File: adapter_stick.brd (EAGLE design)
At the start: 15.2 x 20 mm, 7 parts, among them J1X CLONOLU

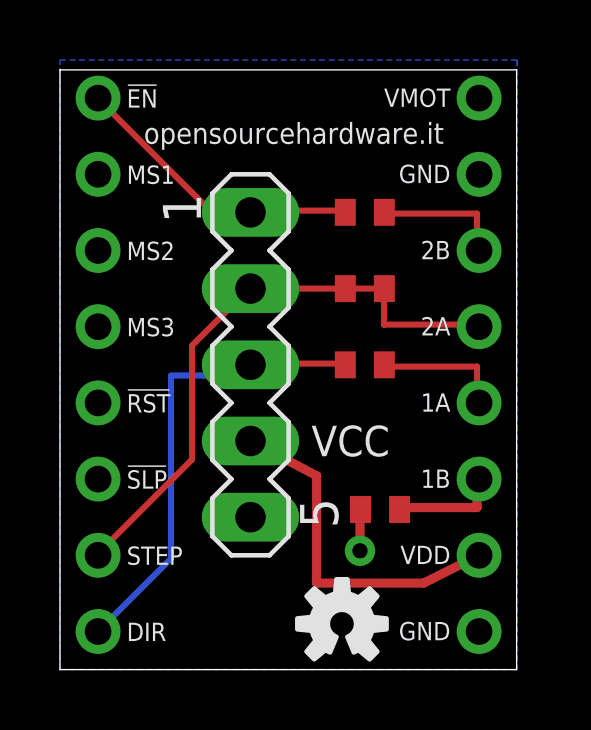
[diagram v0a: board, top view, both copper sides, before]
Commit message: BUG in board (DIR jumper shorted)
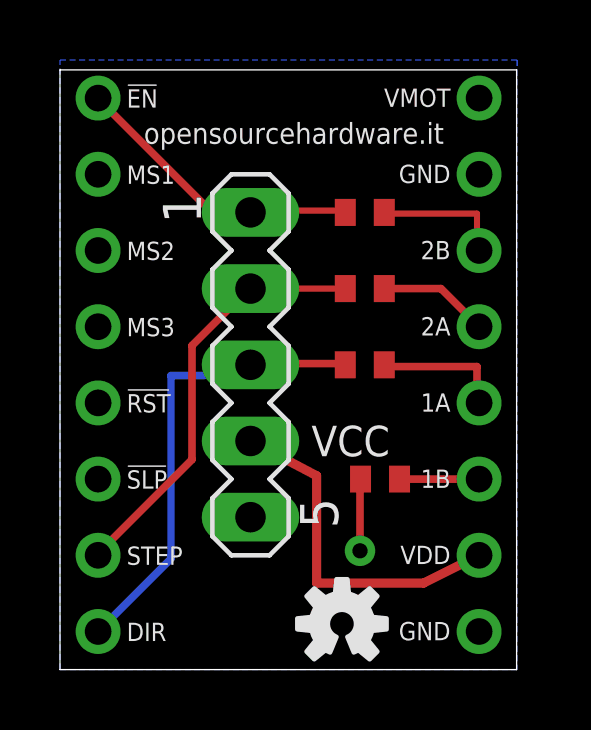
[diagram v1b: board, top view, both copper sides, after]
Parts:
- moved R5 1.02 mm to (10.7, 6.35)
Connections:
- new net 2A: J1X.2A, R3.2
- net NC: no longer J1X.2A, R3.2
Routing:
- net NC: track 19.9 -> 14.2 mm
- net 2A: track 0.00 -> 3.69 mm
- net N$1: track 3.59 -> 2.65 mm
- net GND: track 1.51 -> 2.40 mm
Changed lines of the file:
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@@
 <?xml version="1.0" encoding="utf-8"?>
 <!DOCTYPE eagle SYSTEM "eagle.dtd">
-<eagle version="6.2">
+<eagle version="7.2.0">
 <drawing>
 <settings>
@@
 </class>
 </classes>
-<designrules>
+<designrules name="default">
 <description language="it">&lt;b&gt;EAGLE Design Rules&lt;/b&gt;
 &lt;p&gt;
@@
 <pass name="Default">
 <param name="RoutingGrid" value="0.1mm"/>
+<param name="AutoGrid" value="1"/>
+<param name="Efforts" value="0"/>
+<param name="TopRouterVariant" value="1"/>
 <param name="tpViaShape" value="round"/>
 <param name="PrefDir.1" value="|"/>
@@
 <attribute name="VALUE" x="8.255" y="10.795" size="1.016" layer="27"/>
 </element>
-<element name="R5" library="rcl" package="R0402" value="GND" x="10.668" y="5.334" smashed="yes">
+<element name="R5" library="rcl" package="R0402" value="GND" x="10.668" y="6.35" smashed="yes">
 <attribute name="VALUE" x="4.953" y="2.413" size="1.016" layer="27"/>
 </element>
@@
 <vertex x="0" y="0"/>
 </polygon>
-<wire x1="10" y1="3.96" x2="10" y2="5.4" width="0.3048" layer="1"/>
-<wire x1="10" y1="5.4" x2="10.018" y2="5.334" width="0.2032" layer="1"/>
 <via x="10" y="3.96" extent="1-16" drill="0.508"/>
+<wire x1="10" y1="3.96" x2="10" y2="6.332" width="0.254" layer="1"/>
+<wire x1="10" y1="6.332" x2="10.018" y2="6.35" width="0.254" layer="1"/>
 </signal>
 <signal name="EN">
@@
 <wire x1="9.5" y1="15.3" x2="9.51" y2="15.24" width="0.2032" layer="1"/>
 <wire x1="6.4" y1="15.3" x2="6.35" y2="15.24" width="0.2032" layer="1"/>
-<wire x1="5" y1="15.3" x2="1.3" y2="19" width="0.2032" layer="1"/>
+<wire x1="5" y1="15.3" x2="1.3" y2="19" width="0.254" layer="1"/>
 <wire x1="6.3" y1="15.3" x2="5" y2="15.3" width="0.2032" layer="1"/>
 <wire x1="1.3" y1="19" x2="1.27" y2="19.05" width="0.2032" layer="1"/>
@@
 </signal>
 <signal name="NC">
-<contactref element="J1X" pad="2A"/>
 <contactref element="SV1" pad="2"/>
-<contactref element="R3" pad="2"/>
 <contactref element="J1X" pad="STEP"/>
 <contactref element="R3" pad="1"/>
-<wire x1="10.81" y1="12.7" x2="9.51" y2="12.7" width="0.2032" layer="1"/>
 <wire x1="6.35" y1="12.7" x2="9.51" y2="12.7" width="0.2032" layer="1"/>
-<wire x1="4.4" y1="7" x2="1.3" y2="3.9" width="0.2032" layer="1"/>
-<wire x1="4.4" y1="10.8" x2="4.4" y2="7" width="0.2032" layer="1"/>
-<wire x1="6.3" y1="12.7" x2="4.4" y2="10.8" width="0.2032" layer="1"/>
+<wire x1="4.4" y1="7" x2="1.3" y2="3.9" width="0.254" layer="1"/>
+<wire x1="4.4" y1="10.8" x2="4.4" y2="7" width="0.254" layer="1"/>
+<wire x1="6.3" y1="12.7" x2="4.4" y2="10.8" width="0.254" layer="1"/>
 <wire x1="1.3" y1="3.9" x2="1.27" y2="3.81" width="0.2032" layer="1"/>
 <wire x1="6.3" y1="12.7" x2="6.35" y2="12.7" width="0.2032" layer="1"/>
-<wire x1="10.8" y1="11.5" x2="13.9" y2="11.5" width="0.2032" layer="1"/>
-<wire x1="10.8" y1="12.6" x2="10.8" y2="11.5" width="0.2032" layer="1"/>
-<wire x1="13.9" y1="11.5" x2="13.97" y2="11.43" width="0.2032" layer="1"/>
-<wire x1="10.8" y1="12.6" x2="10.81" y2="12.7" width="0.2032" layer="1"/>
 </signal>
 <signal name="DIR">
@@
 <contactref element="SV1" pad="3"/>
 <contactref element="R4" pad="1"/>
-<wire x1="6.4" y1="10.2" x2="9.5" y2="10.2" width="0.2032" layer="1"/>
+<wire x1="6.4" y1="10.2" x2="9.5" y2="10.2" width="0.254" layer="1"/>
 <wire x1="9.5" y1="10.2" x2="9.51" y2="10.16" width="0.2032" layer="1"/>
 <wire x1="6.4" y1="10.2" x2="6.35" y2="10.16" width="0.2032" layer="1"/>
-<wire x1="3.7" y1="3.7" x2="1.27" y2="1.27" width="0.2032" layer="16"/>
-<wire x1="3.7" y1="9.8" x2="3.7" y2="3.7" width="0.2032" layer="16"/>
-<wire x1="4.8" y1="9.8" x2="3.7" y2="9.8" width="0.2032" layer="16"/>
+<wire x1="3.7" y1="3.7" x2="1.27" y2="1.27" width="0.254" layer="16"/>
+<wire x1="3.7" y1="9.8" x2="3.7" y2="3.7" width="0.254" layer="16"/>
+<wire x1="4.8" y1="9.8" x2="3.7" y2="9.8" width="0.254" layer="16"/>
 <wire x1="5.1" y1="10.1" x2="4.8" y2="9.8" width="0.2032" layer="16"/>
 <wire x1="6.3" y1="10.1" x2="5.1" y2="10.1" width="0.2032" layer="16"/>
@@
 <contactref element="J1X" pad="1B"/>
 <contactref element="R5" pad="2"/>
-<wire x1="13.9" y1="5.4" x2="11.4" y2="5.4" width="0.3048" layer="1"/>
-<wire x1="13.9" y1="6.3" x2="13.9" y2="5.4" width="0.3048" layer="1"/>
-<wire x1="11.4" y1="5.4" x2="11.318" y2="5.334" width="0.2032" layer="1"/>
-<wire x1="13.9" y1="6.3" x2="13.97" y2="6.35" width="0.2032" layer="1"/>
+<wire x1="11.318" y1="6.35" x2="13.97" y2="6.35" width="0.254" layer="1"/>
 </signal>
 <signal name="N$2">
 <contactref element="J1X" pad="1A"/>
 <contactref element="R4" pad="2"/>
-<wire x1="13.9" y1="10.1" x2="10.9" y2="10.1" width="0.2032" layer="1"/>
-<wire x1="13.9" y1="8.9" x2="13.9" y2="10.1" width="0.2032" layer="1"/>
+<wire x1="13.9" y1="10.1" x2="10.9" y2="10.1" width="0.254" layer="1"/>
+<wire x1="13.9" y1="8.9" x2="13.9" y2="10.1" width="0.254" layer="1"/>
 <wire x1="10.9" y1="10.1" x2="10.81" y2="10.16" width="0.2032" layer="1"/>
 <wire x1="13.9" y1="8.9" x2="13.97" y2="8.89" width="0.2032" layer="1"/>
@@
 <wire x1="13.9" y1="14" x2="13.97" y2="13.97" width="0.2032" layer="1"/>
 </signal>
+<signal name="2A">
+<contactref element="J1X" pad="2A"/>
+<contactref element="R3" pad="2"/>
+<wire x1="10.81" y1="12.7" x2="12.7" y2="12.7" width="0.254" layer="1"/>
+<wire x1="12.7" y1="12.7" x2="13.97" y2="11.43" width="0.254" layer="1"/>
+</signal>
 </signals>
